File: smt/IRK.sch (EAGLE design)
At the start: 37 parts, among them IC1 PIC18F25K50, IC2 MAX4066ESD, Q1 MMBT2222A, Q2 MMBT3906, U1 TSOP4838

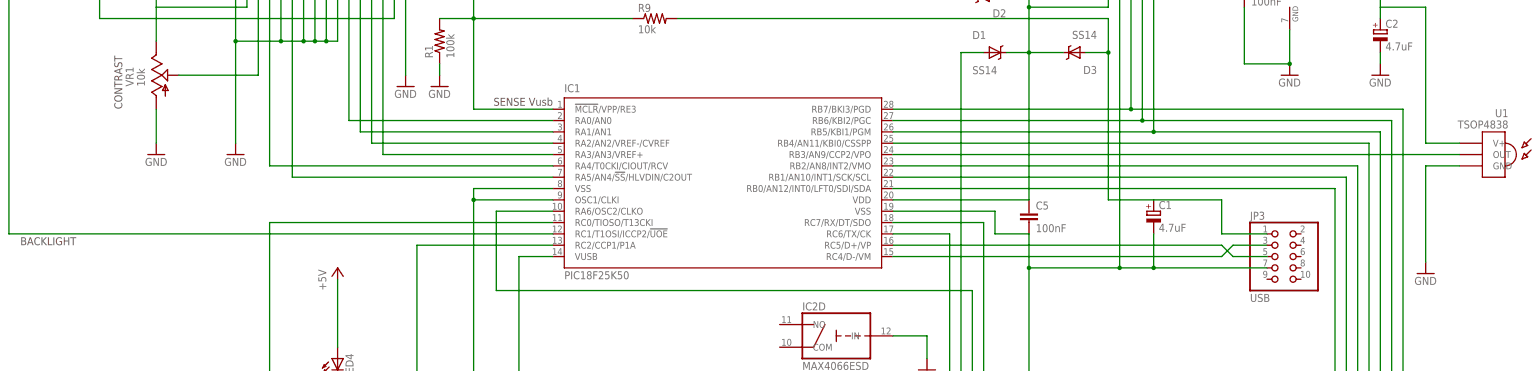
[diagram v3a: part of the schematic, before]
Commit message: Replaced old 2550 device with P18F25K50 in IRK.lbr
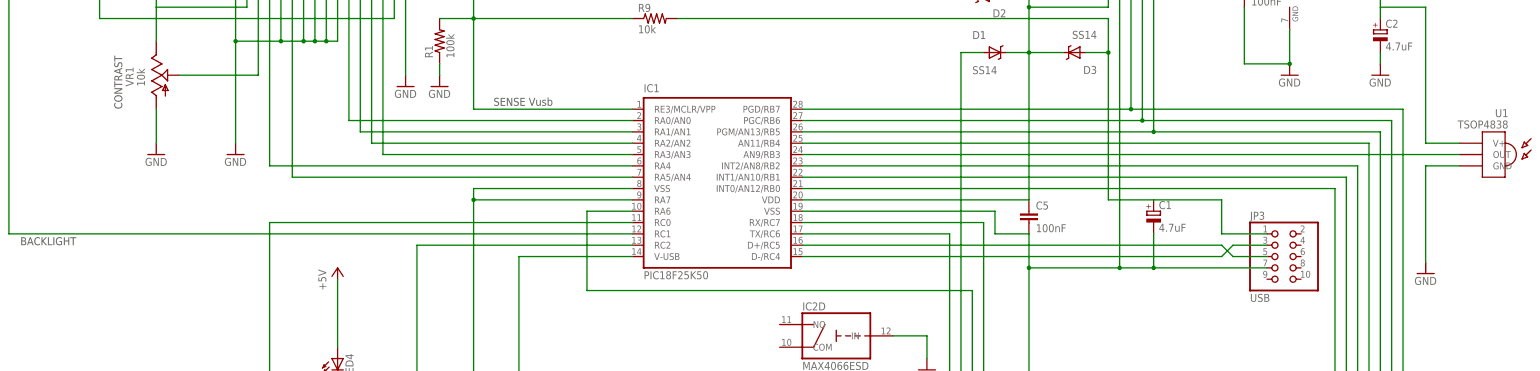
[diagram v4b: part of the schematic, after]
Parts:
- IC1: device microchip:PIC18F2550_28W -> irk:PIC18F25K50SO28W
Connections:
- net AUX: now also IC1.RA6; no longer IC1.RA6/OSC2/CLKO
- net GND: now also IC1.RA7, IC1.VSS@19; no longer IC1.OSC1/CLKI, IC1.VSS@1
- net N$10: now also IC1.AN9/RB3; no longer IC1.RB3/AN9/CCP2/VPO
- net N$12: now also IC1.PGD/RB7; no longer IC1.RB7/BKI3/PGD
- net N$13: now also IC1.PGC/RB6; no longer IC1.RB6/KBI2/PGC
- net N$14: now also IC1.PGM/AN13/RB5; no longer IC1.RB5/KBI1/PGM
- net N$15: now also IC1.AN11/RB4; no longer IC1.RB4/AN11/KBI0/CSSPP
- net N$16: now also IC1.INT2/AN8/RB2; no longer IC1.RB2/AN8/INT2/VMO
- net N$17: now also IC1.INT1/AN10/RB1; no longer IC1.RB1/AN10/INT1/SCK/SCL
- net N$18: now also IC1.INT0/AN12/RB0; no longer IC1.RB0/AN12/INT0/LFT0/SDI/SDA
- net N$19: now also IC1.V-USB; no longer IC1.VUSB
- net N$23: now also IC1.D+/RC5; no longer IC1.RC5/D+/VP
- net N$24: now also IC1.D-/RC4; no longer IC1.RC4/D-/VM
- net N$28: now also IC1.RC2; no longer IC1.RC2/CCP1/P1A
- net N$3: now also IC1.RA2/AN2; no longer IC1.RA2/AN2/VREF-/CVREF
- net N$34: now also IC1.RC1; no longer IC1.RC1/T1OSI/ICCP2/!UOE
- net N$4: now also IC1.RA3/AN3; no longer IC1.RA3/AN3/VREF+
- net N$46: now also IC1.RC0; no longer IC1.RC0/TIOSO/T13CKI
- net N$5: now also IC1.RA4; no longer IC1.RA4/T0CKI/CIOUT/RCV
- net N$6: now also IC1.RA5/AN4; no longer IC1.RA5/AN4/!SS!/HLVDIN/C2OUT
- net N$8: now also IC1.RE3/MCLR/VPP; no longer IC1.!MCLR!/VPP/RE3
- net PWR: now also IC1.TX/RC6; no longer IC1.RC6/TX/CK
- net RST: now also IC1.RX/RC7; no longer IC1.RC7/RX/DT/SDO
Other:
- moved on the sheet: IC1

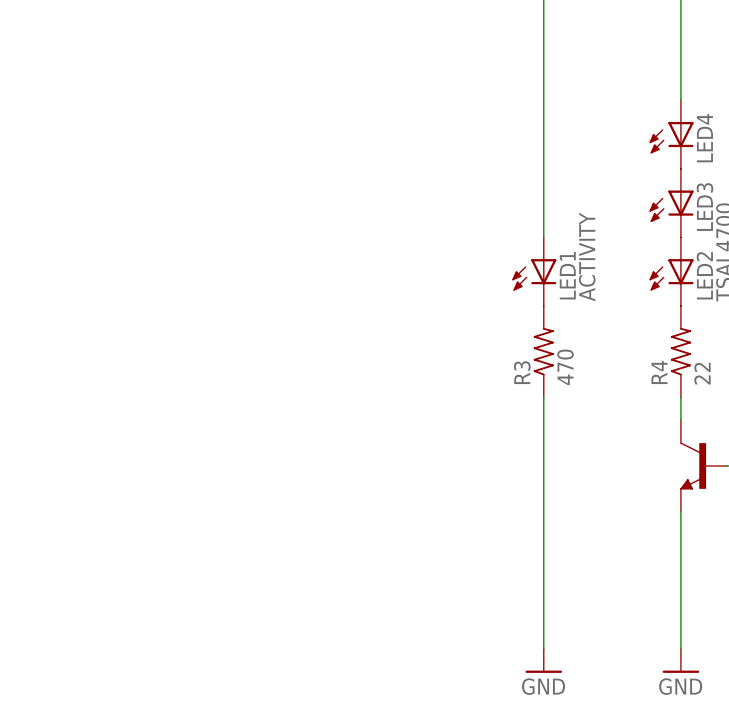
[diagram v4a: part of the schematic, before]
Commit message: Spaced the holes for the IR TX and Activity LEDs at 0.1 inch intervals.
Now (if you want) you can solder a 12x1 pin socket header and plug
your IR TX and Activity LEDs into it rather than soldering them
directly to the board. Long term reliability might be an issue
as the leads oxidise though. The interspersed pin sockets appear on
the schematic as grounded 1x1 header pins.

The IR RX LED has remained slightly offset from the others, because it
needs to be bent 90° so that it is perpendicular to the board.

The board version is now 2.01 as a result of these minor layout changes
and the Gerber files have been regenerated.
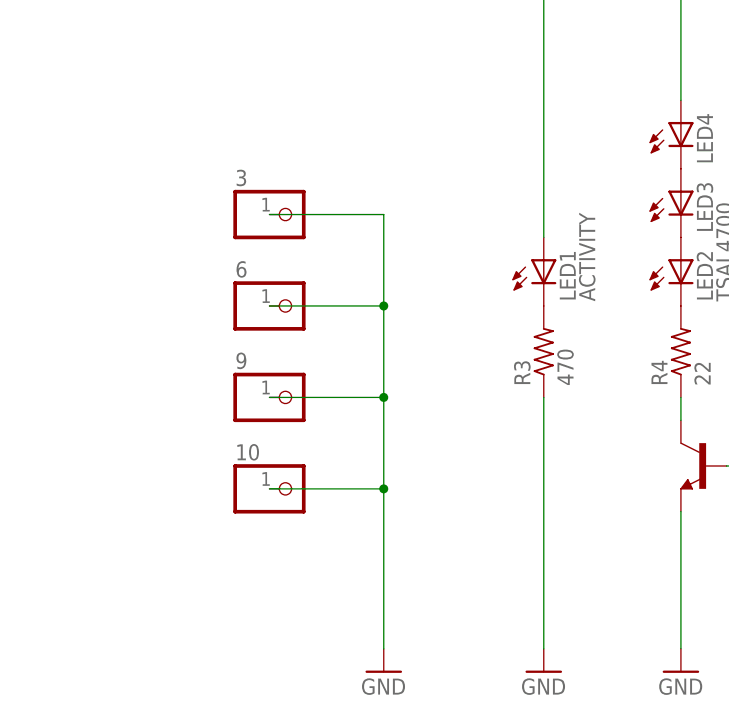
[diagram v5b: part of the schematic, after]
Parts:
- added 10, 3, 6, 9: (no value), pinhead:PINHD-1X1
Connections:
- net GND: now also 10.1, 3.1, 6.1, 9.1
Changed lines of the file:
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@@
 <layer number="91" name="Nets" color="2" fill="1" visible="yes" active="yes"/>
 <layer number="92" name="Busses" color="1" fill="1" visible="yes" active="yes"/>
-<layer number="93" name="Pins" color="2" fill="1" visible="no" active="yes"/>
+<layer number="93" name="Pins" color="2" fill="1" visible="yes" active="yes"/>
 <layer number="94" name="Symbols" color="4" fill="1" visible="yes" active="yes"/>
 <layer number="95" name="Names" color="7" fill="1" visible="yes" active="yes"/>
@@
 <part name="U1" library="irk" deviceset="TSOP4838" device=""/>
 <part name="IC1" library="irk" deviceset="PIC18F25K50" device="SO28W" value="PIC18F25K50"/>
+<part name="3" library="pinhead" deviceset="PINHD-1X1" device="" value=" "/>
+<part name="6" library="pinhead" deviceset="PINHD-1X1" device="" value=" "/>
+<part name="9" library="pinhead" deviceset="PINHD-1X1" device="" value=" "/>
+<part name="10" library="pinhead" deviceset="PINHD-1X1" device="" value=" "/>
+<part name="GND5" library="supply1" deviceset="GND" device=""/>
 </parts>
 <sheets>
@@
 <instance part="U1" gate="&gt;G$1" x="251.46" y="53.34" rot="MR0"/>
 <instance part="IC1" gate="G$1" x="78.74" y="45.72"/>
+<instance part="3" gate="G$1" x="-50.8" y="-2.54"/>
+<instance part="6" gate="G$1" x="-50.8" y="-12.7"/>
+<instance part="9" gate="G$1" x="-50.8" y="-22.86"/>
+<instance part="10" gate="G$1" x="-50.8" y="-33.02"/>
+<instance part="GND5" gate="1" x="-40.64" y="-53.34"/>
 </instances>
 <busses>
@@
 <wire x1="205.74" y1="73.66" x2="205.74" y2="81.28" width="0.1524" layer="91"/>
 </segment>
-</net>
+<segment>
+<pinref part="3" gate="G$1" pin="1"/>
+<wire x1="-40.64" y1="-33.02" x2="-40.64" y2="-22.86" width="0.1524" layer="91"/>
+<wire x1="-40.64" y1="-22.86" x2="-40.64" y2="-12.7" width="0.1524" layer="91"/>
+<wire x1="-40.64" y1="-12.7" x2="-40.64" y2="-2.54" width="0.1524" layer="91"/>
+<wire x1="-40.64" y1="-2.54" x2="-53.34" y2="-2.54" width="0.1524" layer="91"/>
+<pinref part="10" gate="G$1" pin="1"/>
+<wire x1="-53.34" y1="-33.02" x2="-40.64" y2="-33.02" width="0.1524" layer="91"/>
+<pinref part="6" gate="G$1" pin="1"/>
+<wire x1="-53.34" y1="-12.7" x2="-40.64" y2="-12.7" width="0.1524" layer="91"/>
+<junction x="-40.64" y="-12.7"/>
+<pinref part="9" gate="G$1" pin="1"/>
+<wire x1="-53.34" y1="-22.86" x2="-40.64" y2="-22.86" width="0.1524" layer="91"/>
+<junction x="-40.64" y="-22.86"/>
+<pinref part="GND5" gate="1" pin="GND"/>
+<wire x1="-40.64" y1="-50.8" x2="-40.64" y2="-33.02" width="0.1524" layer="91"/>
+<junction x="-40.64" y="-33.02"/>
+</segment>
+</net>
